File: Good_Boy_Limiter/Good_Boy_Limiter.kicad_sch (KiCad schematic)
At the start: 15 parts, among them J1 Out, Q2 AO3422, U1 ESP32-S3-WROOM-1, U2 TC4427EOA_C636891, U3 XL7015E1

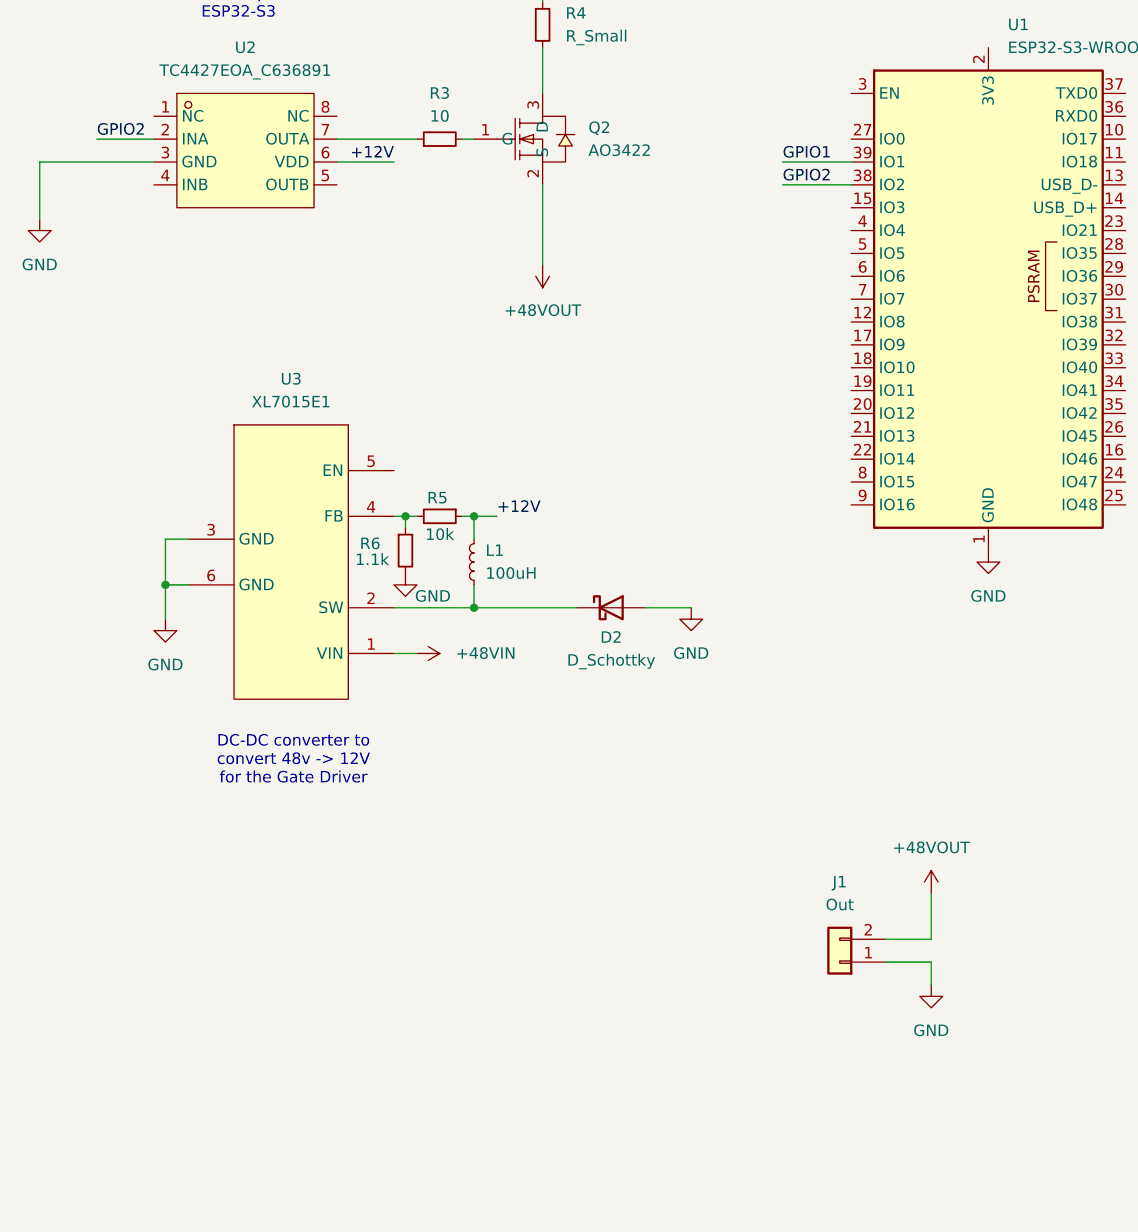
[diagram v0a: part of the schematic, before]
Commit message: Added schottky and Inductor for DC-DC converter
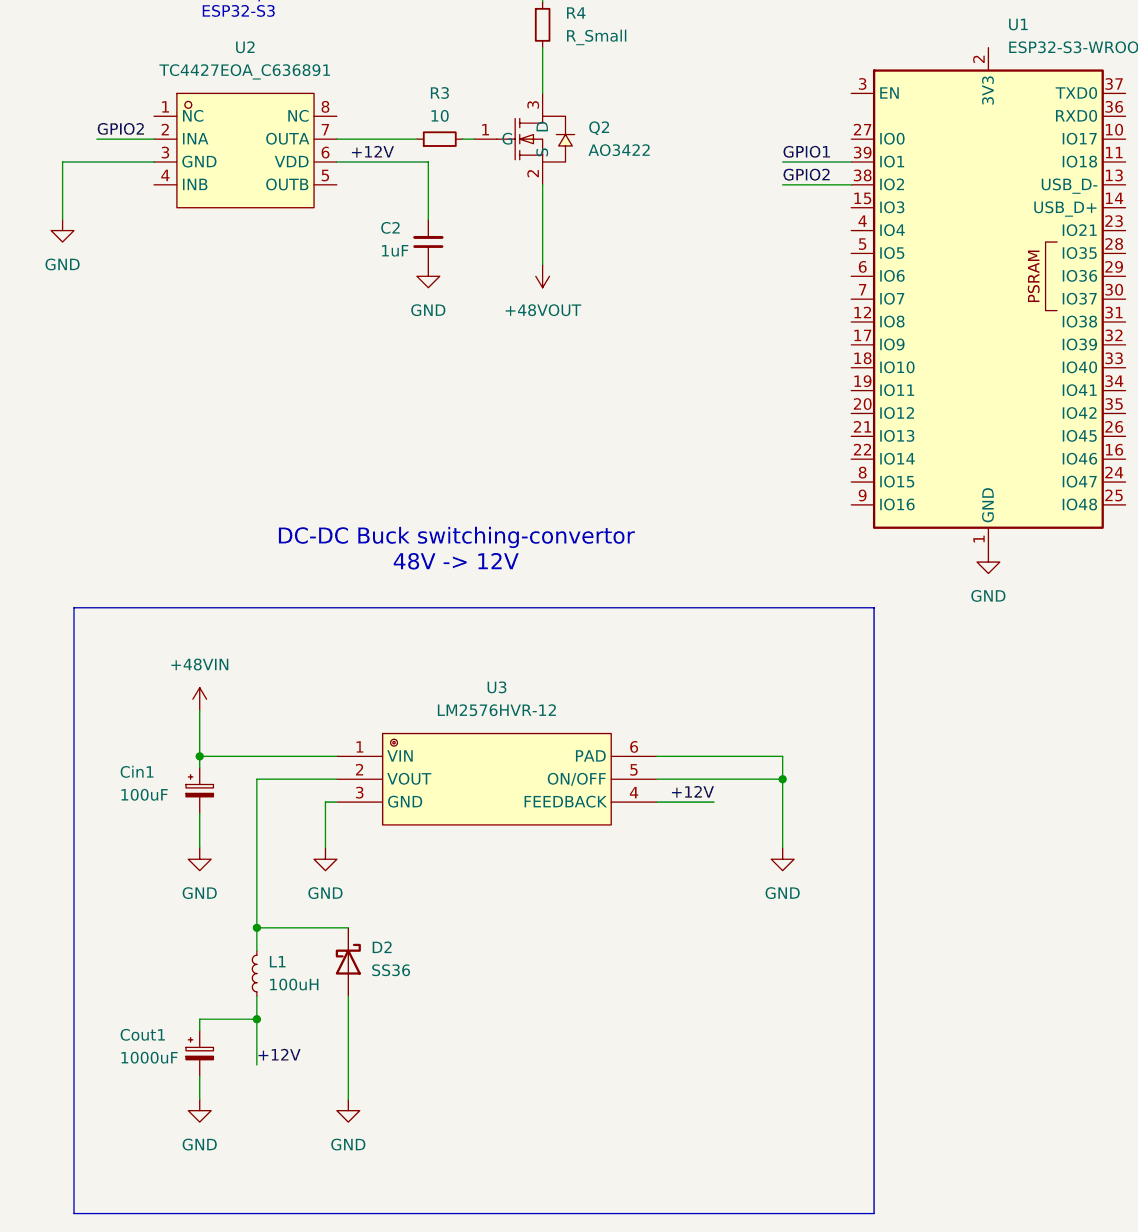
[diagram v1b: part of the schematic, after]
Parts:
- removed J1: Out, symbol Connector_Generic:Conn_01x02
- removed R5: 10k, symbol Device:R_Small
- removed R6: 1.1k, symbol Device:R_Small
- removed U3: XL7015E1, easyeda2kicad:TO-252-5_L6.6-W5.8-P1.27-TL, symbol easyeda2kicad:XL7015E1
- added C2: 1uF, symbol Device:C_Small
- added Cin1: 100uF, symbol Device:C_Polarized_Small
- added Cout1: 1000uF, symbol Device:C_Polarized_Small
- added U3: LM2576HVR-12, easyeda2kicad:TO-263-5_L10.2-W8.6-P1.70-LS14.4-TL, symbol easyeda2kicad:LM2576HVR-12
- D2: value D_Schottky -> SS36; footprint (none) -> Diode_SMD:D_SMA_Handsoldering; LCSC Part (none) -> C16015
- L1: LCSC Part (none) -> C22463856
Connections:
- net +12V: now also L1.1, C2.2, Cout1.1, U3.4 (FEEDBACK); no longer L1.2
- net +48VIN: now also Cin1.1, U3.1 (VIN)
- net GND: now also C2.1, Cin1.2, Cout1.2, U3.3 (GND), U3.5 (ON/OFF), U3.6 (PAD)
- net at D2.1 (K): now also L1.2, U3.2 (VOUT); no longer L1.1
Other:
- note added: "DC-DC Buck switching-convertor 48V -> 12V"
- note removed: "DC-DC converter to convert 48v -> 12V for the Gate Driver"

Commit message: FIX: Added capacitors for Buck
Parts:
- removed L1: 100uH, symbol Device:L_Small
- added L2: SL1050-101M, easyeda2kicad:IND-SMD_L11.5-W10.5, symbol easyeda2kicad:SL1050-101M
- Cin1: footprint (none) -> easyeda2kicad:CAP-SMD_BD16.0-L17.0-W17.0-FD
- Cout1: footprint (none) -> easyeda2kicad:CAP-SMD_BD10.0-L10.3-W10.3-FD
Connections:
- net +12V: now also L2.1
- net at D2.1 (K), U3.2 (VOUT): now also L2.2
- no-connect marks 0 -> 2
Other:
- note added: "Pre-charge Switch"
- moved on the sheet: Cout1, U1

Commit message: Added a lot of stuff, sowwy
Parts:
- added C3, C5, C6: 100nF, symbol Device:C_Small
- added C4: 10uF, symbol Device:C_Small
- added D7, D8: LED, LED_SMD:LED_0805_2012Metric_Pad1.15x1.40mm_HandSolder, symbol Device:LED
- added R10, R11: 330, symbol Device:R
- added R5: 10k, symbol Device:R
- added SW1: RESET1, symbol Switch:SW_Push
- added SW2: BOOT1, symbol Switch:SW_Push
- added U9: LM393DR2G, easyeda2kicad:SOIC-8_L5.0-W4.0-P1.27-LS6.0-BL, symbol easyeda2kicad:LM393DR2G
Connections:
- net GND: now also C3.2, C4.2, C5.2, C6.2, SW1.1, SW2.1, U9.4 (GND)
- net D-: now reaches U1.13 (USB_D-)
- net D+: now reaches U1.14 (USB_D+)
- net 3V3: now reaches U1.2 (3V3)
- net 3V3: now also C3.1, C4.1, R10.2, R11.1, R5.1, U9.8 (VCC)
- net GPIO0: now reaches U1.27 (IO0)
- net GPIO0: now also C6.1, SW2.2
- net at U1.3 (EN): now also C5.1, R5.2, SW1.2
- new net: D8.2 (A), R11.2
- new net: D7.1 (K), U9.1 (OUT/A)
- new net: D7.2 (A), R10.1
- new net: D8.1 (K), U9.7 (OUT/B)
- new net 3V3Buck: U9.3 (IN/A), U9.6 (IN/B/2)
- new net 3V3LDO: U9.2 (IN/A/2), U9.5 (IN/B)
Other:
- added sheet DC-DC Buck 12V-3V3 (12V_to_3V3.kicad_sch)
- added sheet USB Communication (USB_communication.kicad_sch)
- note added: "LEDs to check which alimentation is delivering"
- moved on the sheet: C1, D1, R1, R2, U1

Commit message: Added some footprints
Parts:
- R10, R11: footprint (none) -> LED_SMD:LED_0805_2012Metric_Pad1.15x1.40mm_HandSolder; LCSC Part (none) -> C17630
- R3: footprint (none) -> LED_SMD:LED_0805_2012Metric_Pad1.15x1.40mm_HandSolder; LCSC Part (none) -> C17415
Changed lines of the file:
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@@
 			)
 		)
-		(property "Footprint" ""
+		(property "Footprint" "LED_SMD:LED_0805_2012Metric_Pad1.15x1.40mm_HandSolder"
 			(at 259.08 148.082 90)
 			(effects
@@
 			)
 		)
+		(property "LCSC Part" "C17630"
+			(at 259.08 149.86 0)
+			(effects
+				(font
+					(size 1.27 1.27)
+				)
+				(hide yes)
+			)
+		)
 		(pin "2"
 		)
@@
 			)
 		)
-		(property "Footprint" ""
+		(property "Footprint" "LED_SMD:LED_0805_2012Metric_Pad1.15x1.40mm_HandSolder"
 			(at 62.23 67.31 0)
 			(effects
@@
 			)
 		)
+		(property "LCSC Part" "C17415"
+			(at 62.23 67.31 0)
+			(effects
+				(font
+					(size 1.27 1.27)
+				)
+				(hide yes)
+			)
+		)
 		(pin "1"
 		)
@@
 			)
 		)
-		(property "Footprint" ""
+		(property "Footprint" "LED_SMD:LED_0805_2012Metric_Pad1.15x1.40mm_HandSolder"
 			(at 172.72 145.542 90)
 			(effects
@@
 			(at 172.72 147.32 0)
 			(effects
+				(font
+					(size 1.27 1.27)
+				)
+				(hide yes)
+			)
+		)
+		(property "LCSC Part" "C17630"
+			(at 172.72 147.32 0)
+			(effects

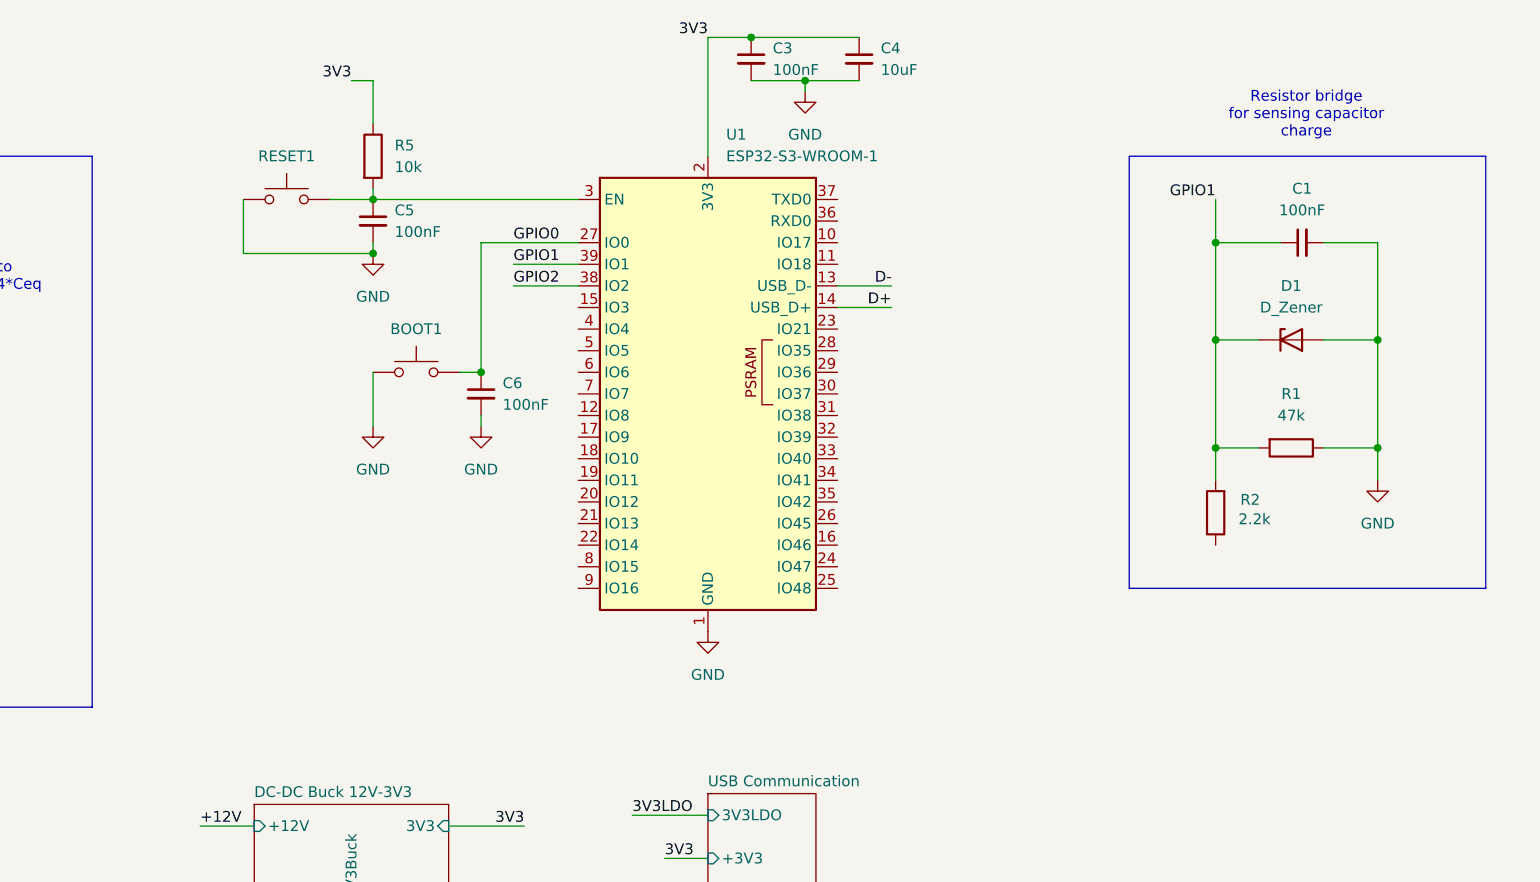
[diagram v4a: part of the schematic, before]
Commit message: Added more footprints
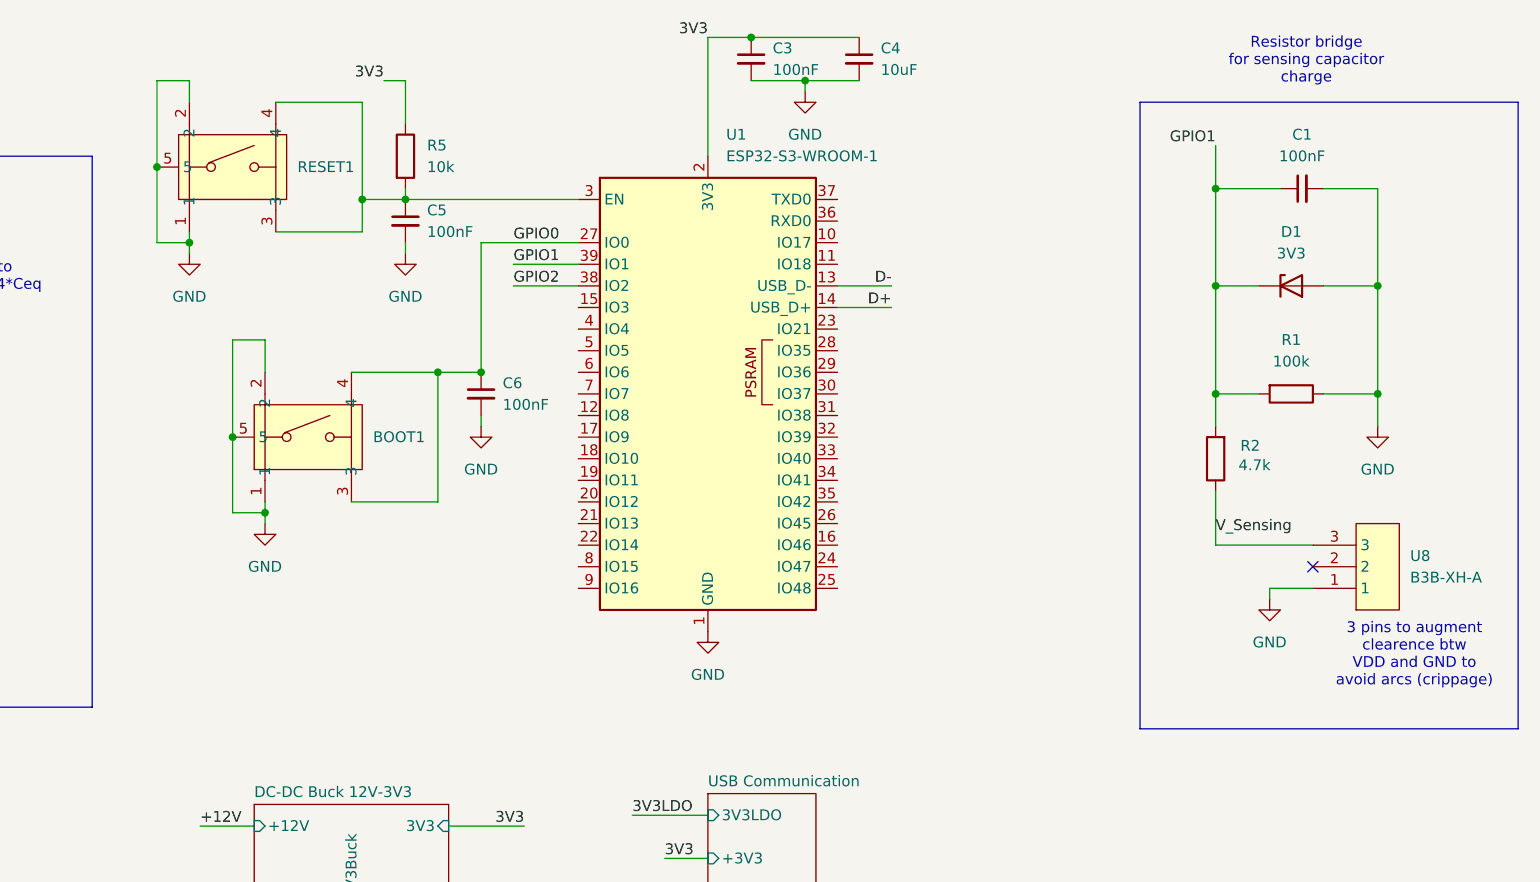
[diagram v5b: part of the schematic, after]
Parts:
- removed D1: D_Zener, symbol Device:D_Zener
- removed SW1: RESET1, symbol Switch:SW_Push
- removed SW2: BOOT1, symbol Switch:SW_Push
- added D1: 3V3, Package_TO_SOT_SMD:SOT-23, symbol Diode:BZX84Cxx
- added SW3: RESET1, easyeda2kicad:KEY-SMD_KMR2XXGXXX, symbol easyeda2kicad:KMR221GLFS
- added SW4: BOOT1, easyeda2kicad:KEY-SMD_KMR2XXGXXX, symbol easyeda2kicad:KMR221GLFS
- added U8: B3B-XH-A, easyeda2kicad:CONN-TH_3P-P2.50_A2501WV2-3P, symbol easyeda2kicad:B3B-XH-A
- R1: value 47k -> 100k; LCSC Part (none) -> C177329
- R2: value 2.2k -> 4.7k; LCSC Part (none) -> C177333
- R5: footprint (none) -> Resistor_SMD:R_0201_0603Metric_Pad0.64x0.40mm_HandSolder; LCSC Part (none) -> C177337
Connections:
- net GND: now also D1.1 (A), SW3.1, SW3.2, SW3.5, SW4.1, SW4.2, SW4.5, U8.1
- net GPIO0: now also SW4.3, SW4.4
- net GPIO1: now also D1.3 (K)
- net at C5.1, R5.2, U1.3 (EN): now also SW3.3, SW3.4
- net V_Sensing: now reaches R2.1
- net V_Sensing: now also U8.3
- no-connect marks 2 -> 3
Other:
- note added: "3 pins to augment clearence btw VDD and GND to avoid arcs (crippage)"
- moved on the sheet: C1, C5, R1, R2, R5
